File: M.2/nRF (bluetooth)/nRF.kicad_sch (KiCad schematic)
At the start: 21 parts, among them M1 M.2_Key_E, SW101 RESET, U1 MK08, U2 BQ24232HARGTT

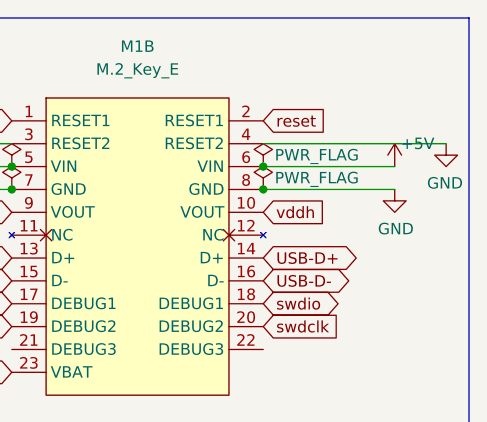
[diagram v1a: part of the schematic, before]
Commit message: change up logo's to nicer ones on modules, update iss
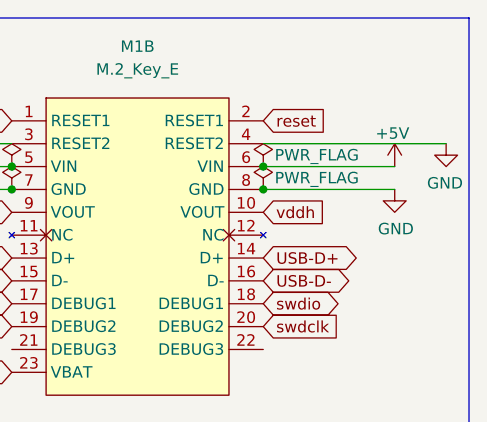
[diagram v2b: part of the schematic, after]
